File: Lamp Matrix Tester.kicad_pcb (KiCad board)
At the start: 2 copper layers, 50.8 x 53.3 mm, 11 parts, among them J1 Columns, J2 Rows, U1 1088AS

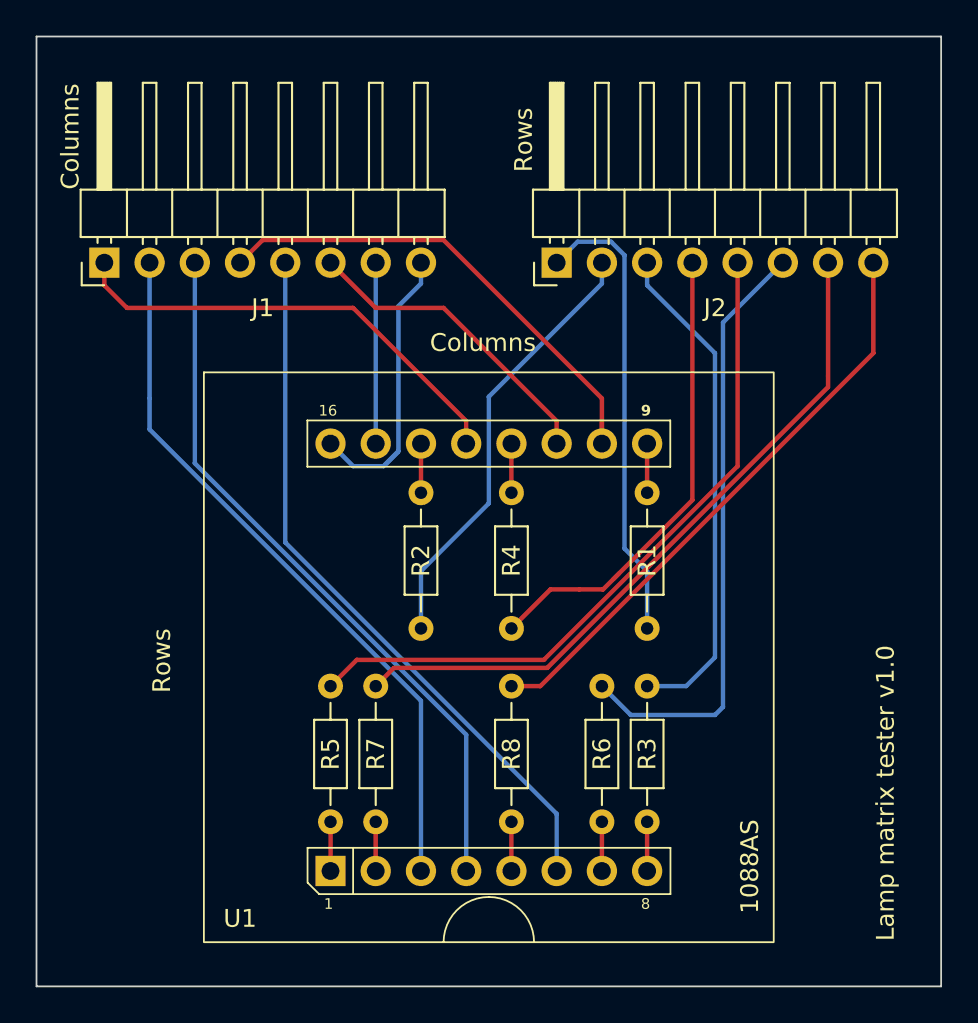
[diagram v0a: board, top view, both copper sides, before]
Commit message: V1.1 - Swapped rows and cols position and pinout
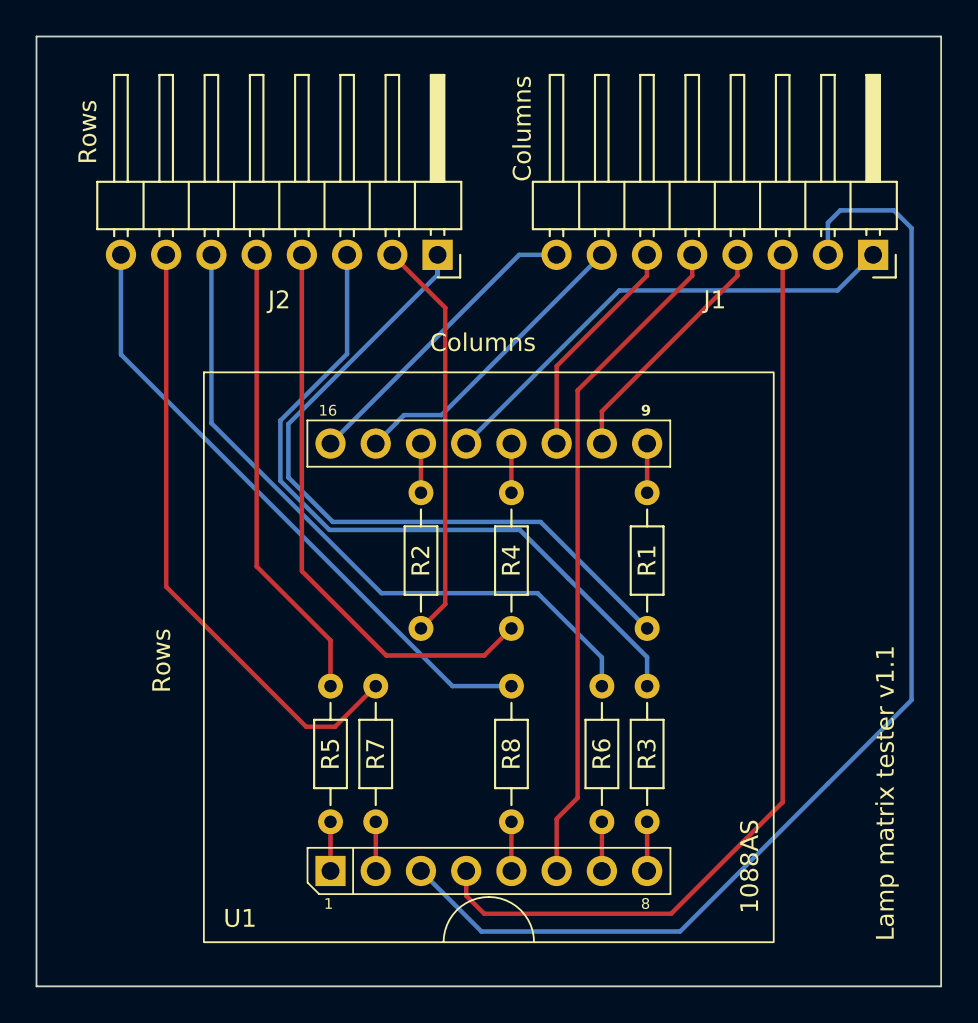
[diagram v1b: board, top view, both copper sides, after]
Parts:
- moved J1 25.4 mm to (52.1, 27.5)
- moved J2 24.5 mm to (27.6, 27.5)
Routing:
- net /Col_2: track 40.5 -> 68.0 mm
- net /Row_1: track 26.1 -> 40.8 mm
- net /Col_4: track 28.3 -> 13.8 mm
- net /Row_5: track 39.4 -> 25.9 mm
- net /Col_3: track 40.5 -> 52.9 mm
- net /Row_3: track 28.2 -> 40.6 mm
- net /Col_7: track 10.2 -> 17.1 mm
- net /Row_4: track 26.9 -> 32.1 mm
- net /Col_6: track 17.7 -> 12.7 mm
- net /Row_7: track 39.3 -> 34.6 mm
- net /Row_6: track 34.0 -> 38.4 mm
- net /Col_5: track 40.5 -> 37.8 mm
- net /Row_8: track 33.1 -> 35.2 mm
- net /Row_2: track 24.7 -> 22.8 mm
- net /Col_1: track 26.0 -> 27.2 mm
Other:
- board text added: "Lamp matrix tester v1.1"
- board text removed: "Lamp matrix tester v1.0"
